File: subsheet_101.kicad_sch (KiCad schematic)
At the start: 5 parts, among them J305 No Blitter, U101 ST_BLITTER_PHY

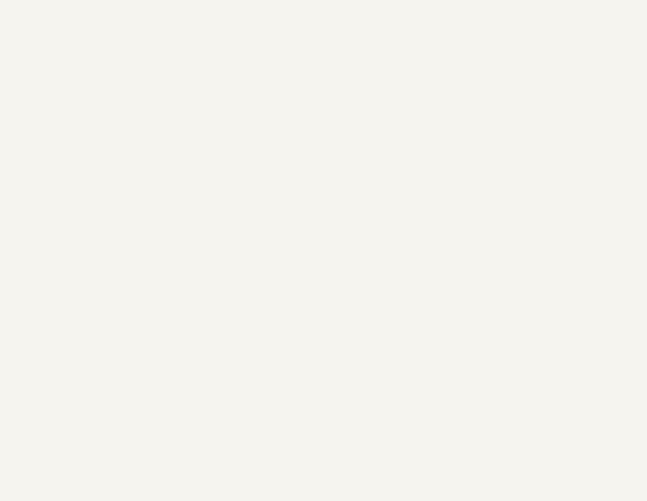
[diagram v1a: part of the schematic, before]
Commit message: add gnd/vcc symbol to start replacing local labels
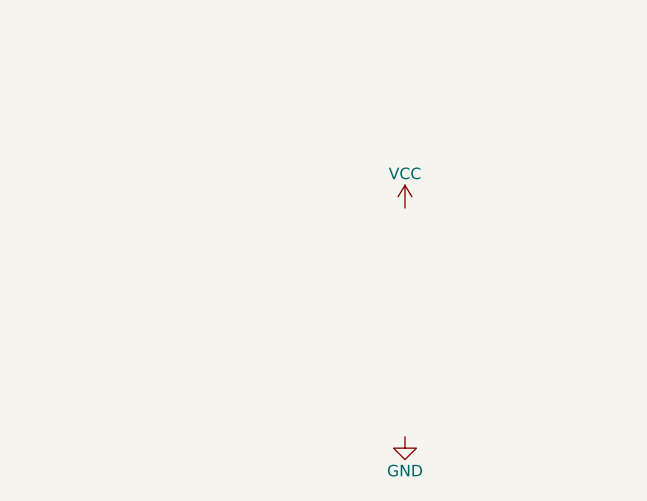
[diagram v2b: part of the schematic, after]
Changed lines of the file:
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@@
     (pin "4")
   )
+  (symbol (lib_id "power:GND") (at 166.37 210.82 0) (unit 1)
+    (in_bom yes) (on_board yes)
+    (property "Reference" "#PWR?" (id 0) (at 166.37 217.17 0)
+      (effects (font (size 1.27 1.27)) hide)
+    )
+    (property "Value" "GND" (id 1) (at 166.37 214.63 0))
+    (property "Footprint" "" (id 2) (at 166.37 210.82 0)
+      (effects (font (size 1.27 1.27)) hide)
+    )
+    (property "Datasheet" "" (id 3) (at 166.37 210.82 0)
+      (effects (font (size 1.27 1.27)) hide)
+    )
+    (pin "1")
+  )
+  (symbol (lib_id "power:VCC") (at 166.37 185.42 0) (unit 1)
+    (in_bom yes) (on_board yes)
+    (property "Reference" "#PWR?" (id 0) (at 166.37 189.23 0)
+      (effects (font (size 1.27 1.27)) hide)
+    )
+    (property "Value" "VCC" (id 1) (at 166.37 181.61 0))
+    (property "Footprint" "" (id 2) (at 166.37 185.42 0)
+      (effects (font (size 1.27 1.27)) hide)
+    )
+    (property "Datasheet" "" (id 3) (at 166.37 185.42 0)
+      (effects (font (size 1.27 1.27)) hide)
+    )
+    (pin "1")
+  )
 )
